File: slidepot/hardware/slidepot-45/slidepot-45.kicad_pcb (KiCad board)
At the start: 2 copper layers, 17.8 x 92.7 mm, 3 parts, among them J1 Conn_01x05_Male, J2 Conn_01x02

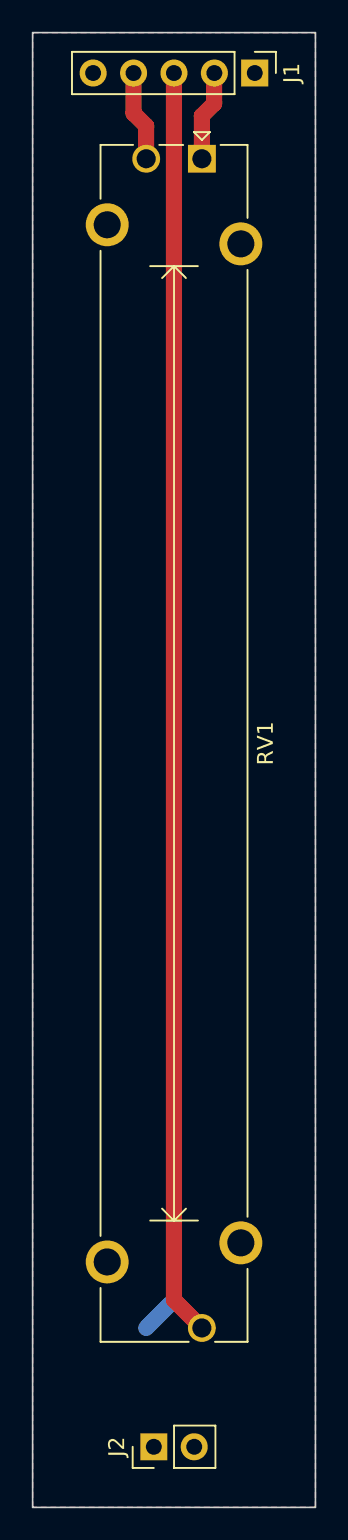
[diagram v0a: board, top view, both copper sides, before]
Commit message: Update slideot-45 footprint
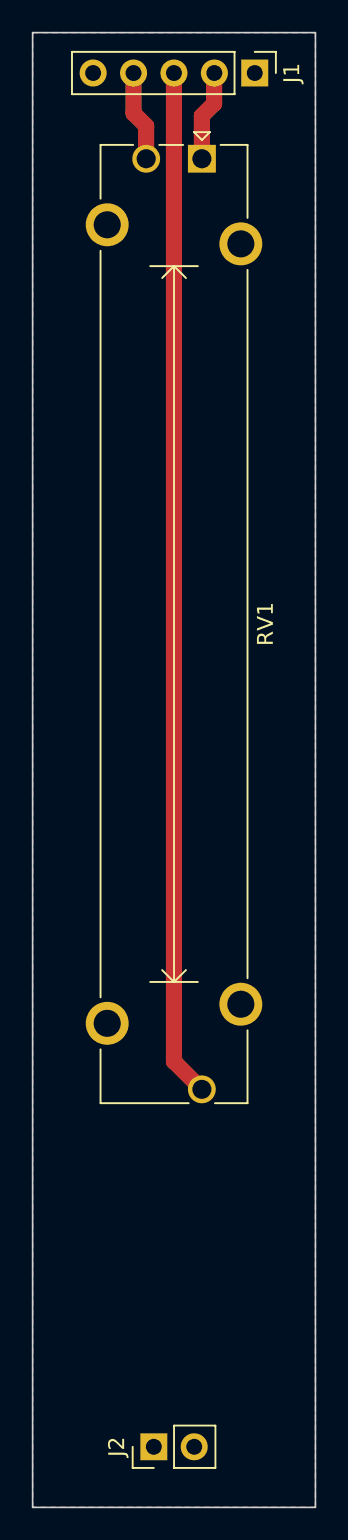
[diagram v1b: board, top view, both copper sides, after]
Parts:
- RV1: footprint Potentiometer_THT:Potentiometer_Bourns_PTA6043_Single_Slide -> Potentiometer_THT:Potentiometer_Bourns_PTA4543_Single_Slide
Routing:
- net Net-(J1-Pad3): track 79.6 -> 64.6 mm
- net GND: track 2.47 -> 0.00 mm

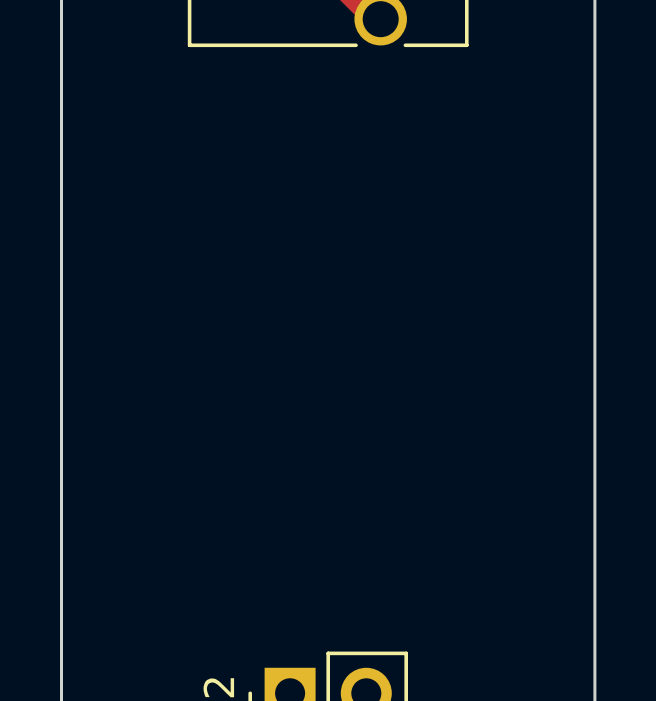
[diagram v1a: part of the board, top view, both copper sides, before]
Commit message: Assign part numbers
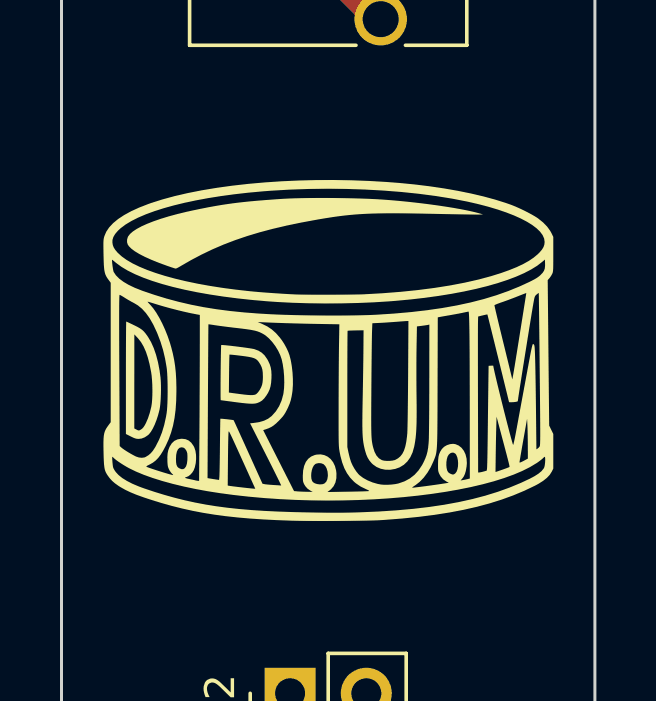
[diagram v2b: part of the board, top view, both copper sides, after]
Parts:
- added G***: LOGO, LOGO, F.Cu at (165.1, 120.7)
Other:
- board text added: "D.R.U.M. Slidepot 45mm Riser HW Design REV: 1.0 Layout REV: A Order No. P/N DRUM-SR-1045"
